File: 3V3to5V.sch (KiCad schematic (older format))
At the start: 5 parts, among them U3 74AHCT367, U4 74AHCT367

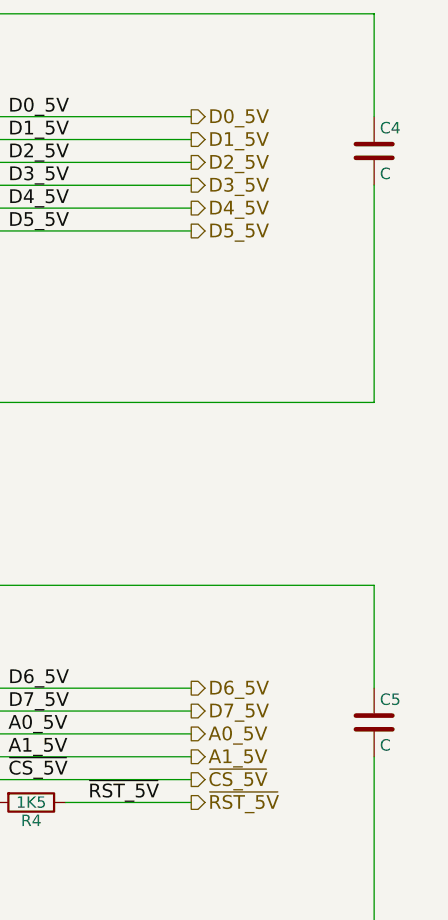
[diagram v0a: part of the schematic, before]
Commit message: Added connectors for LCD to the schematics
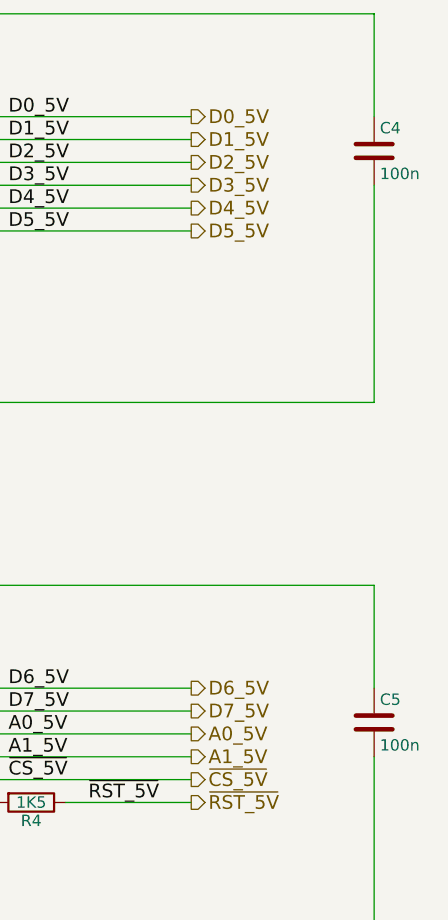
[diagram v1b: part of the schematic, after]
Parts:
- C4, C5: value C -> 100n; Manufacturer (none) -> Multicomp; Order Code (none) -> 1759166; Part Number (none) -> MC0805B104K250CT
- U3, U4: Alt. Order Code (none) -> 595-SN74AHCT367D; Alt. Supplier (none) -> Mouser; Note (none) -> Hex buffer and line driver with 3-state output; Order Code 1749633 -> 1740954; Package (none) -> SOIC-16; Part Number SN74AHCT367PW -> SN74AHCT367D; Supplier (none) -> Farnell
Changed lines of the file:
@@
 F 2 "Housings_SOIC:SOIC-16_3.9x9.9mm_Pitch1.27mm" H 3400 2500 50  0001 C CNN
 F 3 "" H 3400 2500 50  0000 C CNN
-F 4 "SN74AHCT367PW" H 3400 2500 60  0001 C CNN "Part Number"
+F 4 "SN74AHCT367D" H 3400 2500 60  0001 C CNN "Part Number"
 F 5 "Texas Instruments" H 3400 2500 60  0001 C CNN "Manufacturer"
-F 6 "1749633" H 3400 2500 60  0001 C CNN "Order Code"
+F 6 "SOIC-16" H 3400 2500 60  0001 C CNN "Package"
+F 7 "Farnell" H 3400 2500 60  0001 C CNN "Supplier"
+F 8 "1740954" H 3400 2500 60  0001 C CNN "Order Code"
+F 9 "Mouser" H 3400 2500 60  0001 C CNN "Alt. Supplier"
+F 10 "595-SN74AHCT367D" H 3400 2500 60  0001 C CNN "Alt. Order Code"
+F 11 "Hex buffer and line driver with 3-state output" H 3400 2500 60  0001 C CNN "Note"
 	1    3400 2500
 	1    0    0    -1
@@
 P 5800 2250
 F 0 "C4" H 5825 2350 50  0000 L CNN
-F 1 "C" H 5825 2150 50  0000 L CNN
+F 1 "100n" H 5825 2150 50  0000 L CNN
 F 2 "Capacitors_SMD:C_0805" H 5838 2100 50  0001 C CNN
 F 3 "" H 5800 2250 50  0000 C CNN
+F 4 "MC0805B104K250CT" H 5800 2250 60  0001 C CNN "Part Number"
+F 5 "Multicomp" H 5800 2250 60  0001 C CNN "Manufacturer"
+F 6 "1759166" H 5800 2250 60  0001 C CNN "Order Code"
 	1    5800 2250
 	1    0    0    -1
@@
 P 5800 4750
 F 0 "C5" H 5825 4850 50  0000 L CNN
-F 1 "C" H 5825 4650 50  0000 L CNN
+F 1 "100n" H 5825 4650 50  0000 L CNN
 F 2 "Capacitors_SMD:C_0805" H 5838 4600 50  0001 C CNN
 F 3 "" H 5800 4750 50  0000 C CNN
+F 4 "MC0805B104K250CT" H 5800 4750 60  0001 C CNN "Part Number"
+F 5 "Multicomp" H 5800 4750 60  0001 C CNN "Manufacturer"
+F 6 "1759166" H 5800 4750 60  0001 C CNN "Order Code"
 	1    5800 4750
 	1    0    0    -1
@@
 $Comp
 L 74AHCT367 U4
-U 1 1 5674E951
+U 1 1 56C786D8
 P 3400 5000
 F 0 "U4" H 3400 5050 50  0000 C CNN
@@
 F 2 "Housings_SOIC:SOIC-16_3.9x9.9mm_Pitch1.27mm" H 3400 5000 50  0001 C CNN
 F 3 "" H 3400 5000 50  0000 C CNN
-F 4 "SN74AHCT367PW" H 3400 5000 60  0001 C CNN "Part Number"
+F 4 "SN74AHCT367D" H 3400 5000 60  0001 C CNN "Part Number"
 F 5 "Texas Instruments" H 3400 5000 60  0001 C CNN "Manufacturer"
-F 6 "1749633" H 3400 5000 60  0001 C CNN "Order Code"
+F 6 "SOIC-16" H 3400 5000 60  0001 C CNN "Package"
+F 7 "Farnell" H 3400 5000 60  0001 C CNN "Supplier"
+F 8 "1740954" H 3400 5000 60  0001 C CNN "Order Code"
+F 9 "Mouser" H 3400 5000 60  0001 C CNN "Alt. Supplier"
+F 10 "595-SN74AHCT367D" H 3400 5000 60  0001 C CNN "Alt. Order Code"
+F 11 "Hex buffer and line driver with 3-state output" H 3400 5000 60  0001 C CNN "Note"
 	1    3400 5000
 	1    0    0    -1

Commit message: Renamed files, added part description
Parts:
- C4, C5: Alt. Order Code (none) -> 710-885012207098; Alt. Supplier (none) -> Mouser; Note (none) -> 100nF/50V X7R 0805 ceramic capacitor; Package (none) -> 0805; Supplier (none) -> Farnell
- R4: Alt. Order Code (none) -> 71-CRCW0805-1.5K-E3; Alt. Supplier (none) -> Mouser; Note (none) -> 1.5kΩ/1% 0805 resistor; Package (none) -> 0805; Supplier (none) -> Farnell
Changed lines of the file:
@@
 LIBS:valves
 LIBS:jakub
-LIBS:MicroFLiC_LCD_1_0-cache
+LIBS:MicroFLiC_LCD-cache
 EELAYER 25 0
 EELAYER END
@@
 F 4 "MC0805B104K250CT" H 5800 2250 60  0001 C CNN "Part Number"
 F 5 "Multicomp" H 5800 2250 60  0001 C CNN "Manufacturer"
-F 6 "1759166" H 5800 2250 60  0001 C CNN "Order Code"
+F 6 "0805" H 5800 2250 60  0001 C CNN "Package"
+F 7 "Farnell" H 5800 2250 60  0001 C CNN "Supplier"
+F 8 "1759166" H 5800 2250 60  0001 C CNN "Order Code"
+F 9 "Mouser" H 5800 2250 60  0001 C CNN "Alt. Supplier"
+F 10 "710-885012207098" H 5800 2250 60  0001 C CNN "Alt. Order Code"
+F 11 "100nF/50V X7R 0805 ceramic capacitor" H 5800 2250 60  0001 C CNN "Note"
 	1    5800 2250
 	1    0    0    -1
@@
 F 4 "MC0805B104K250CT" H 5800 4750 60  0001 C CNN "Part Number"
 F 5 "Multicomp" H 5800 4750 60  0001 C CNN "Manufacturer"
-F 6 "1759166" H 5800 4750 60  0001 C CNN "Order Code"
+F 6 "0805" H 5800 4750 60  0001 C CNN "Package"
+F 7 "Farnell" H 5800 4750 60  0001 C CNN "Supplier"
+F 8 "1759166" H 5800 4750 60  0001 C CNN "Order Code"
+F 9 "Mouser" H 5800 4750 60  0001 C CNN "Alt. Supplier"
+F 10 "710-885012207098" H 5800 4750 60  0001 C CNN "Alt. Order Code"
+F 11 "100nF/50V X7R 0805 ceramic capacitor" H 5800 4750 60  0001 C CNN "Note"
 	1    5800 4750
 	1    0    0    -1
@@
 F 4 "MCWR08X1501FTL" V 4300 5100 60  0001 C CNN "Part Number"
 F 5 "Multicomp" V 4300 5100 60  0001 C CNN "Manufacturer"
-F 6 "2447592" V 4300 5100 60  0001 C CNN "Order Code"
+F 6 "0805" H 4300 5100 60  0001 C CNN "Package"
+F 7 "Farnell" H 4300 5100 60  0001 C CNN "Supplier"
+F 8 "2447592" V 4300 5100 60  0001 C CNN "Order Code"
+F 9 "Mouser" H 4300 5100 60  0001 C CNN "Alt. Supplier"
+F 10 "71-CRCW0805-1.5K-E3" H 4300 5100 60  0001 C CNN "Alt. Order Code"
+F 11 "1.5kΩ/1% 0805 resistor" H 4300 5100 60  0001 C CNN "Note"
 	1    4300 5100
 	0    1    1    0

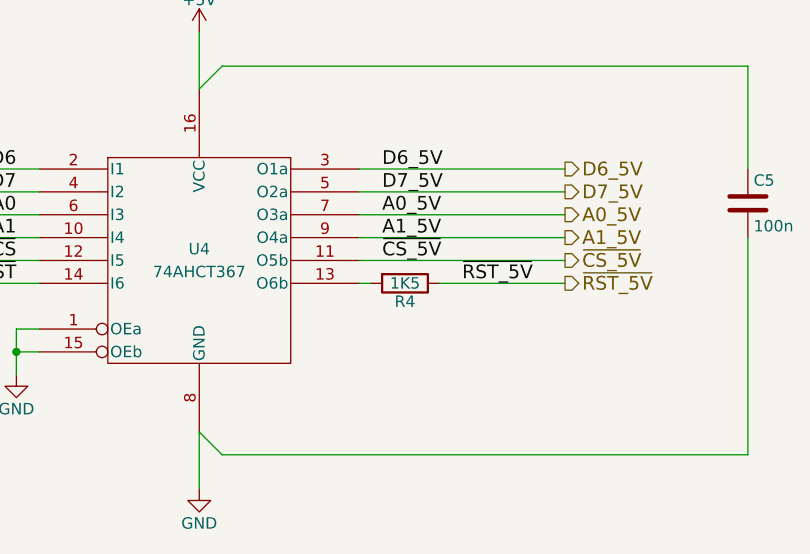
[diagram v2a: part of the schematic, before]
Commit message: Fixed label of 1k5 resistor
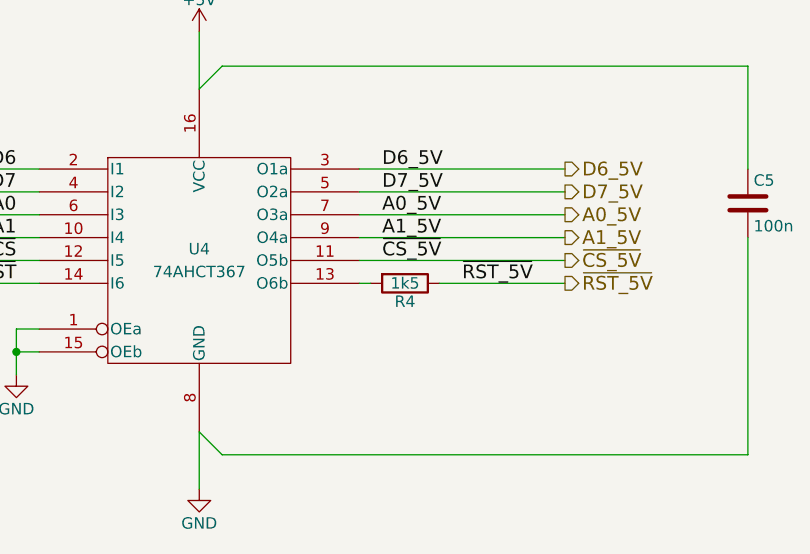
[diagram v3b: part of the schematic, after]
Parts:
- R4: value 1K5 -> 1k5
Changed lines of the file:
@@
 P 4300 5100
 F 0 "R4" V 4380 5100 50  0000 C CNN
-F 1 "1K5" V 4300 5100 50  0000 C CNN
+F 1 "1k5" V 4300 5100 50  0000 C CNN
 F 2 "Resistors_SMD:R_0805" V 4230 5100 50  0001 C CNN
 F 3 "" H 4300 5100 50  0000 C CNN

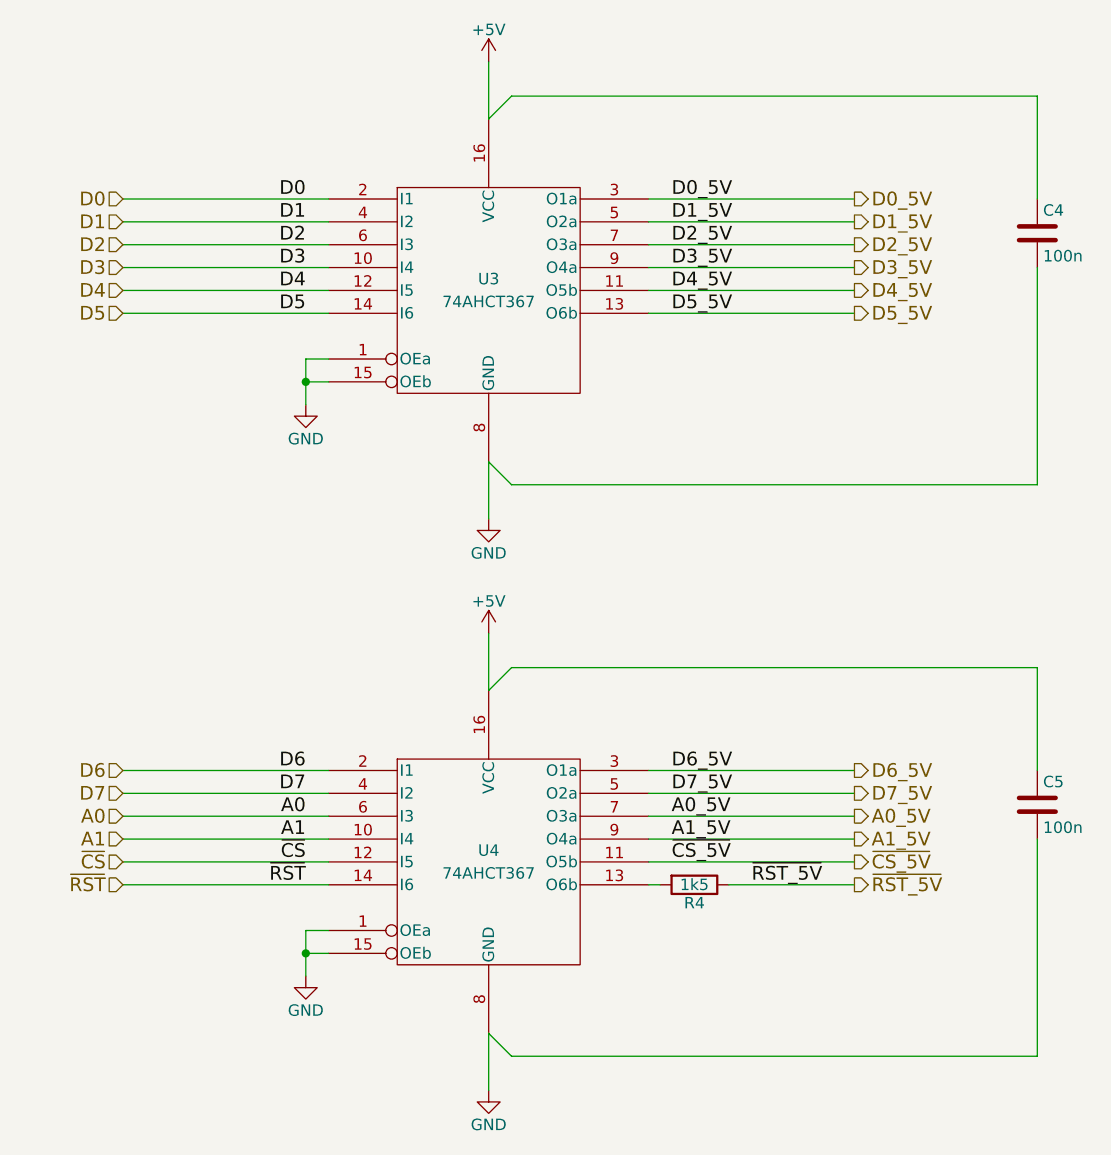
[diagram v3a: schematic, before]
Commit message: Fixed LCD orientation, added powerful emitter-follower amplifier
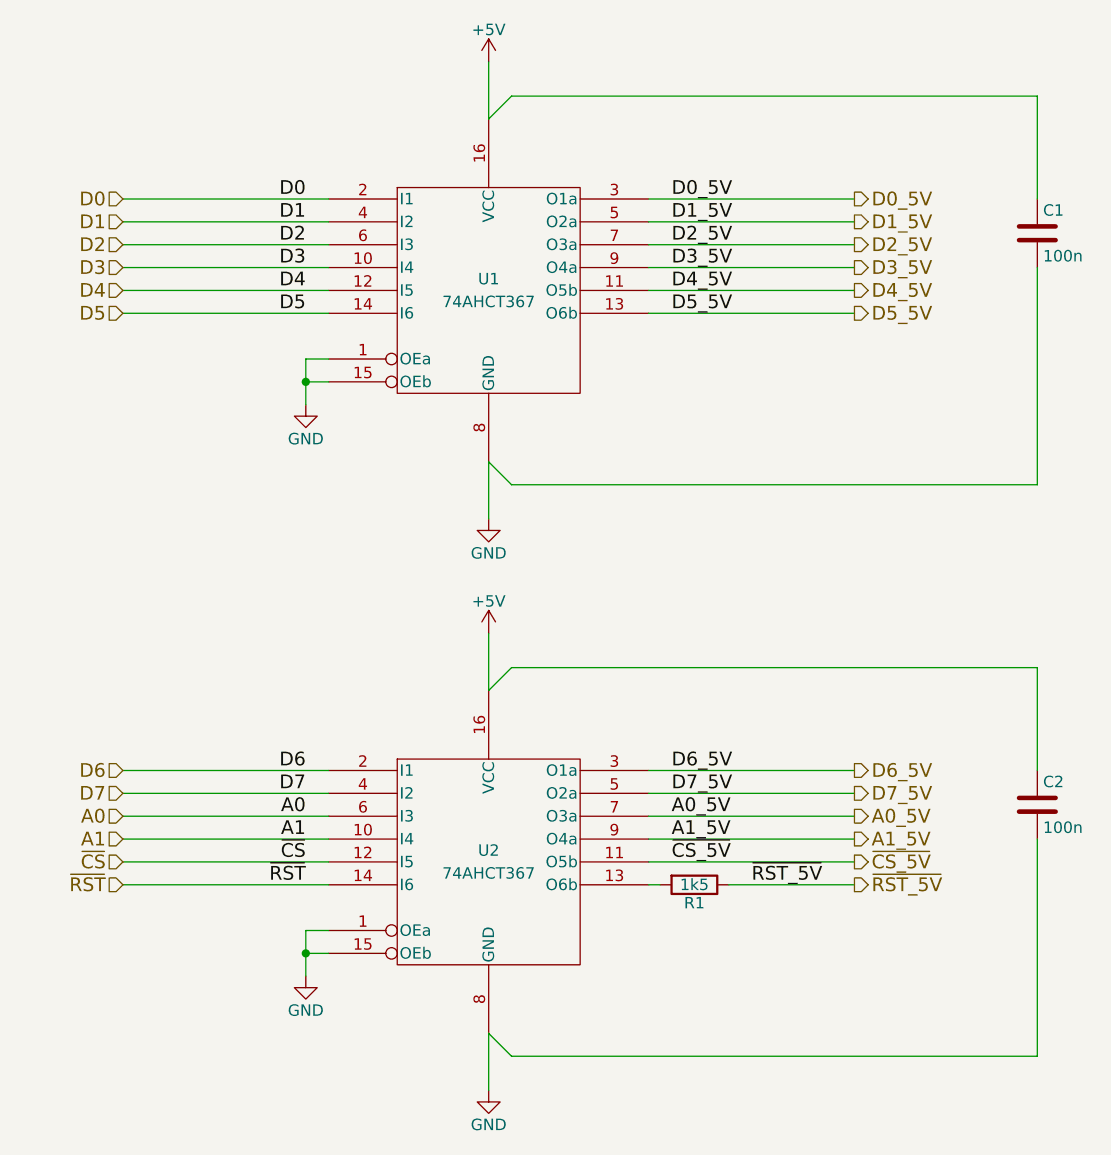
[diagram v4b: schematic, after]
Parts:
- renumbered C4 to C1, C5 to C2, R4 to R1, U3 to U1, U4 to U2
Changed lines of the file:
@@
 $Descr A4 11693 8268
 encoding utf-8
-Sheet 2 2
+Sheet 2 3
 Title ""
 Date ""
@@
 $EndDescr
 $Comp
-L 74AHCT367 U3
+L 74AHCT367 U1
 U 1 1 566F6434
 P 3400 2500
-F 0 "U3" H 3400 2550 50  0000 C CNN
+F 0 "U1" H 3400 2550 50  0000 C CNN
 F 1 "74AHCT367" H 3400 2450 50  0000 C CNN
 F 2 "Housings_SOIC:SOIC-16_3.9x9.9mm_Pitch1.27mm" H 3400 2500 50  0001 C CNN
@@
 $EndComp
 $Comp
-L C C4
+L C C1
 U 1 1 566F6544
 P 5800 2250
-F 0 "C4" H 5825 2350 50  0000 L CNN
+F 0 "C1" H 5825 2350 50  0000 L CNN
 F 1 "100n" H 5825 2150 50  0000 L CNN
 F 2 "Capacitors_SMD:C_0805" H 5838 2100 50  0001 C CNN
@@
 Connection ~ 2600 2900
 $Comp
-L GND #PWR015
+L GND #PWR09
 U 1 1 566F6689
 P 2600 3000
-F 0 "#PWR015" H 2600 2750 50  0001 C CNN
+F 0 "#PWR09" H 2600 2750 50  0001 C CNN
 F 1 "GND" H 2600 2850 50  0000 C CNN
 F 2 "" H 2600 3000 50  0000 C CNN
@@
 	3400 3250 3400 3500
 $Comp
-L GND #PWR016
+L GND #PWR010
 U 1 1 566F66B5
 P 3400 3500
-F 0 "#PWR016" H 3400 3250 50  0001 C CNN
+F 0 "#PWR010" H 3400 3250 50  0001 C CNN
 F 1 "GND" H 3400 3350 50  0000 C CNN
 F 2 "" H 3400 3500 50  0000 C CNN
@@
 	3400 1750 3400 1500
 $Comp
-L +5V #PWR017
+L +5V #PWR011
 U 1 1 566F66DA
 P 3400 1500
-F 0 "#PWR017" H 3400 1350 50  0001 C CNN
+F 0 "#PWR011" H 3400 1350 50  0001 C CNN
 F 1 "+5V" H 3400 1640 50  0000 C CNN
 F 2 "" H 3400 1500 50  0000 C CNN
@@
 D5
 $Comp
-L C C5
+L C C2
 U 1 1 566F689A
 P 5800 4750
-F 0 "C5" H 5825 4850 50  0000 L CNN
+F 0 "C2" H 5825 4850 50  0000 L CNN
 F 1 "100n" H 5825 4650 50  0000 L CNN
 F 2 "Capacitors_SMD:C_0805" H 5838 4600 50  0001 C CNN
@@
 Connection ~ 2600 5400
 $Comp
-L GND #PWR018
+L GND #PWR012
 U 1 1 566F68B7
 P 2600 5500
-F 0 "#PWR018" H 2600 5250 50  0001 C CNN
+F 0 "#PWR012" H 2600 5250 50  0001 C CNN
 F 1 "GND" H 2600 5350 50  0000 C CNN
 F 2 "" H 2600 5500 50  0000 C CNN
@@
 	3400 5750 3400 6000
 $Comp
-L GND #PWR019
+L GND #PWR013
 U 1 1 566F68BE
 P 3400 6000
-F 0 "#PWR019" H 3400 5750 50  0001 C CNN
+F 0 "#PWR013" H 3400 5750 50  0001 C CNN
 F 1 "GND" H 3400 5850 50  0000 C CNN
 F 2 "" H 3400 6000 50  0000 C CNN
@@
 	3400 4250 3400 4000
 $Comp
-L +5V #PWR020
+L +5V #PWR014
 U 1 1 566F68C5
 P 3400 4000
-F 0 "#PWR020" H 3400 3850 50  0001 C CNN
+F 0 "#PWR014" H 3400 3850 50  0001 C CNN
 F 1 "+5V" H 3400 4140 50  0000 C CNN
 F 2 "" H 3400 4000 50  0000 C CNN
@@
 ~RST_5V
 $Comp
-L R R4
+L R R1
 U 1 1 56718BA1
 P 4300 5100
-F 0 "R4" V 4380 5100 50  0000 C CNN
+F 0 "R1" V 4380 5100 50  0000 C CNN
 F 1 "1k5" V 4300 5100 50  0000 C CNN
 F 2 "Resistors_SMD:R_0805" V 4230 5100 50  0001 C CNN
@@
 	4150 5100 4100 5100
 $Comp
-L 74AHCT367 U4
+L 74AHCT367 U2
 U 1 1 56C786D8
 P 3400 5000
-F 0 "U4" H 3400 5050 50  0000 C CNN
+F 0 "U2" H 3400 5050 50  0000 C CNN
 F 1 "74AHCT367" H 3400 4950 50  0000 C CNN
 F 2 "Housings_SOIC:SOIC-16_3.9x9.9mm_Pitch1.27mm" H 3400 5000 50  0001 C CNN
